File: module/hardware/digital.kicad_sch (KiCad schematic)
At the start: 36 parts, among them J10 Conn_01x03, J11 Conn_01x03, J12 Conn_01x03, J5 Conn_01x03_Male, J6 Conn_01x03_Male, J7 Conn_01x03, J8 Conn_01x03, J9 Conn_01x05_Male, SW2 SW_Push, U8 W25Q128JVS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

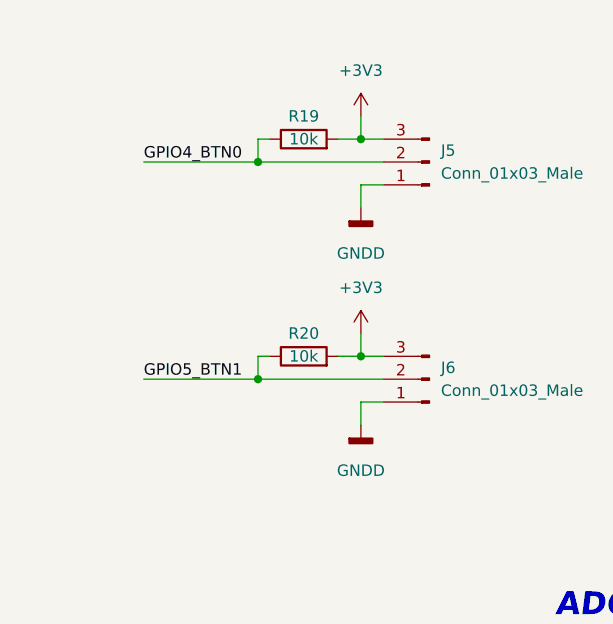
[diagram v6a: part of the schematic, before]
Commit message: Add pull down button resistor option
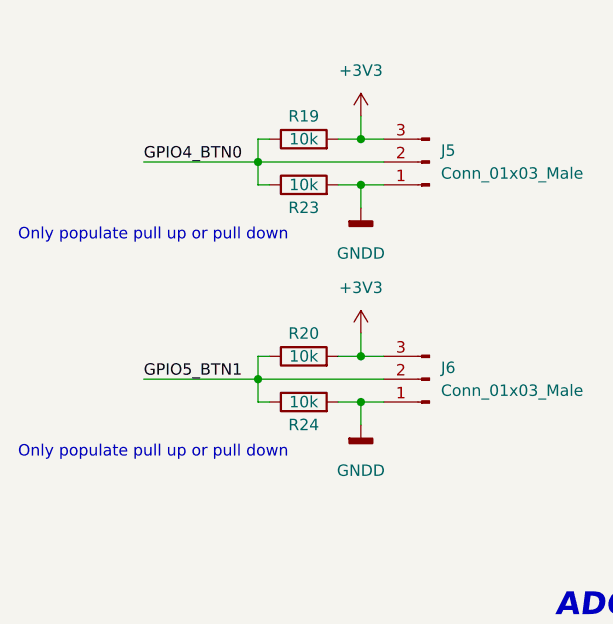
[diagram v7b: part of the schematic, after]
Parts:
- added R23, R24: 10k, Resistor_SMD:R_0603_1608Metric_Pad0.98x0.95mm_HandSolder, symbol Device:R
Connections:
- net GNDD: now also R23.2, R24.2
- net GPIO4_BTN0: now also R23.1
- net GPIO5_BTN1: now also R24.1
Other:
- note added: "Only populate pull up or pull down"
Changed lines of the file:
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@@
   (junction (at 307.34 54.61) (diameter 0) (color 0 0 0 0)
   )
+  (junction (at 69.85 64.77) (diameter 0) (color 0 0 0 0)
+  )
   (junction (at 270.51 40.64) (diameter 0) (color 0 0 0 0)
   )
@@
   )
   (junction (at 78.74 130.81) (diameter 0) (color 0 0 0 0)
+  )
+  (junction (at 69.85 88.9) (diameter 0) (color 0 0 0 0)
   )
   (junction (at 90.17 144.78) (diameter 0) (color 0 0 0 0)
@@
     (stroke (width 0) (type default) (color 0 0 0 0))
   )
+  (wire (pts (xy 58.42 64.77) (xy 59.69 64.77))
+    (stroke (width 0) (type default) (color 0 0 0 0))
+  )
   (wire (pts (xy 114.3 128.27) (xy 127 128.27))
     (stroke (width 0) (type default) (color 0 0 0 0))
@@
     (stroke (width 0) (type default) (color 0 0 0 0))
   )
+  (wire (pts (xy 67.31 88.9) (xy 69.85 88.9))
+    (stroke (width 0) (type default) (color 0 0 0 0))
+  )
   (wire (pts (xy 242.57 52.07) (xy 242.57 55.88))
     (stroke (width 0) (type default) (color 0 0 0 0))
@@
     (stroke (width 0) (type default) (color 0 0 0 0))
   )
+  (wire (pts (xy 58.42 88.9) (xy 59.69 88.9))
+    (stroke (width 0) (type default) (color 0 0 0 0))
+  )
   (wire (pts (xy 242.57 95.25) (xy 233.68 95.25))
     (stroke (width 0) (type default) (color 0 0 0 0))
@@
     (stroke (width 0) (type default) (color 0 0 0 0))
   )
+  (wire (pts (xy 58.42 62.23) (xy 58.42 64.77))
+    (stroke (width 0) (type default) (color 0 0 0 0))
+  )
   (wire (pts (xy 237.49 123.19) (xy 242.57 123.19))
     (stroke (width 0) (type default) (color 0 0 0 0))
@@
     (stroke (width 0) (type default) (color 0 0 0 0))
   )
+  (wire (pts (xy 67.31 64.77) (xy 69.85 64.77))
+    (stroke (width 0) (type default) (color 0 0 0 0))
+  )
   (wire (pts (xy 293.37 85.09) (xy 313.69 85.09))
     (stroke (width 0) (type default) (color 0 0 0 0))
@@
     (stroke (width 0) (type default) (color 0 0 0 0))
   )
+  (wire (pts (xy 58.42 86.36) (xy 58.42 88.9))
+    (stroke (width 0) (type default) (color 0 0 0 0))
+  )
   (wire (pts (xy 275.59 40.64) (xy 278.13 40.64))
     (stroke (width 0) (type default) (color 0 0 0 0))
@@
   (wire (pts (xy 144.78 120.65) (xy 144.78 123.19))
     (stroke (width 0) (type default) (color 0 0 0 0))
+  )
+  (text "Only populate pull up or pull down\n" (at 31.75 71.12 0)
+    (effects (font (size 1.27 1.27)) (justify left bottom))
   )
   (text "Optional fit.\nPlace near ADC headers" (at 71.12 128.27 0)
@@
   )
   (text "Keep routing short" (at 133.35 227.33 0)
+    (effects (font (size 1.27 1.27)) (justify left bottom))
+  )
+  (text "Only populate pull up or pull down\n" (at 31.75 95.25 0)
     (effects (font (size 1.27 1.27)) (justify left bottom))
   )
@@
     (pin "2")
     (pin "3")
+  )
+  (symbol (lib_id "Device:R") (at 63.5 64.77 90) (unit 1)
+    (in_bom yes) (on_board yes)
+    (property "Reference" "R23" (id 0) (at 63.5 67.31 90))
+    (property "Value" "10k" (id 1) (at 63.5 64.77 90))
+    (property "Footprint" "Resistor_SMD:R_0603_1608Metric_Pad0.98x0.95mm_HandSolder" (id 2) (at 63.5 66.548 90)
+      (effects (font (size 1.27 1.27)) hide)
+    )
+    (property "Datasheet" "~" (id 3) (at 63.5 64.77 0)
+      (effects (font (size 1.27 1.27)) hide)
+    )
+    (pin "1")
+    (pin "2")
   )
   (symbol (lib_id "power:+3V3") (at 144.78 120.65 0) (unit 1)
@@
       (effects (font (size 1.27 1.27)) hide)
     )
+    (pin "1")
+    (pin "2")
+  )
+  (symbol (lib_id "Device:R") (at 63.5 88.9 90) (unit 1)
+    (in_bom yes) (on_board yes)
+    (property "Reference" "R24" (id 0) (at 63.5 91.44 90))
+    (property "Value" "10k" (id 1) (at 63.5 88.9 90))
+    (property "Footprint" "Resistor_SMD:R_0603_1608Metric_Pad0.98x0.95mm_HandSolder" (id 2) (at 63.5 90.678 90)
+      (effects (font (size 1.27 1.27)) hide)
+    )
+    (property "Datasheet" "~" (id 3) (at 63.5 88.9 0)
+      (effects (font (size 1.27 1.27)) hide)
+    )

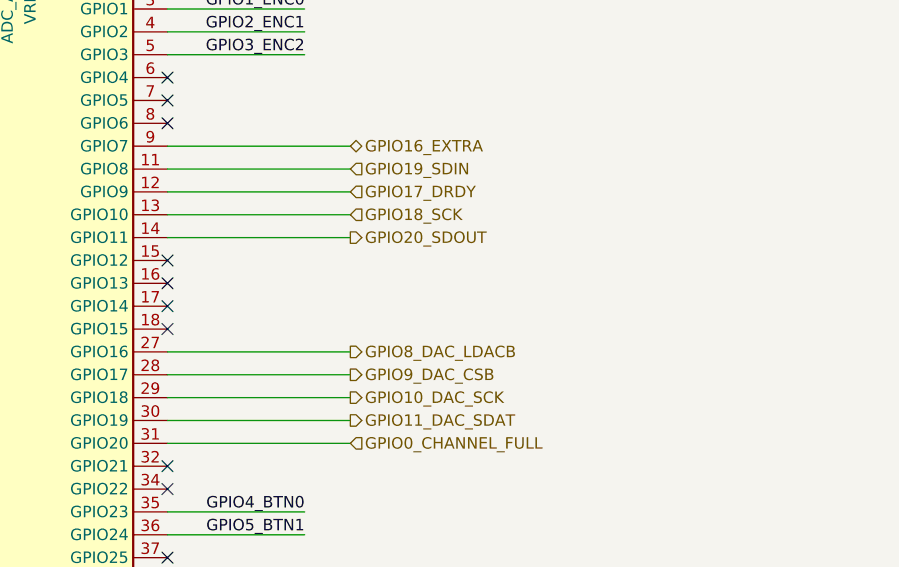
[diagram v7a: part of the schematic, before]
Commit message: Add test points; update silkscreen
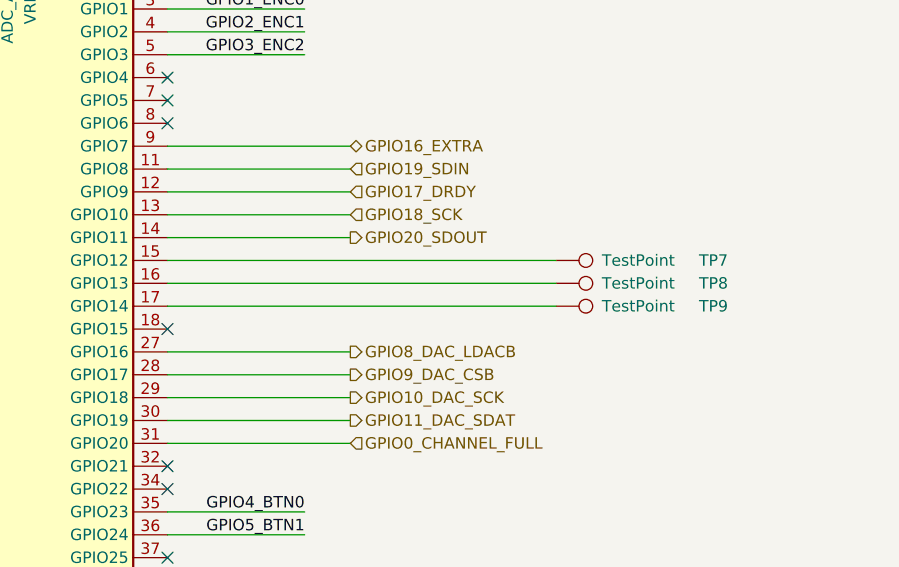
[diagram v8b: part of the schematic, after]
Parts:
- added TP7, TP8, TP9: TestPoint, TestPoint:TestPoint_Pad_D1.5mm, symbol Connector:TestPoint
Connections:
- net at U9.15 (GPIO12): now also TP7.1
- net at U9.16 (GPIO13): now also TP8.1
- net at U9.17 (GPIO14): now also TP9.1
- no-connect marks 11 -> 8
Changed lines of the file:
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@@
   (no_connect (at 293.37 120.65))
   (no_connect (at 293.37 123.19))
-  (no_connect (at 293.37 100.33))
-  (no_connect (at 293.37 97.79))
-  (no_connect (at 293.37 102.87))
   (no_connect (at 293.37 82.55))
   (wire (pts (xy 330.2 40.64) (xy 330.2 44.45))
@@
     (stroke (width 0) (type default) (color 0 0 0 0))
   )
+  (wire (pts (xy 293.37 97.79) (xy 336.55 97.79))
+    (stroke (width 0) (type default) (color 0 0 0 0))
+  )
   (wire (pts (xy 341.63 52.07) (xy 341.63 54.61))
     (stroke (width 0) (type default) (color 0 0 0 0))
@@
     (stroke (width 0) (type default) (color 0 0 0 0))
   )
+  (wire (pts (xy 293.37 100.33) (xy 336.55 100.33))
+    (stroke (width 0) (type default) (color 0 0 0 0))
+  )
   (wire (pts (xy 233.68 74.93) (xy 242.57 74.93))
     (stroke (width 0) (type default) (color 0 0 0 0))
@@
   )
   (wire (pts (xy 275.59 40.64) (xy 278.13 40.64))
+    (stroke (width 0) (type default) (color 0 0 0 0))
+  )
+  (wire (pts (xy 293.37 102.87) (xy 336.55 102.87))
     (stroke (width 0) (type default) (color 0 0 0 0))
   )
@@
     (pin "1")
   )
+  (symbol (lib_id "Connector:TestPoint") (at 336.55 97.79 270) (unit 1)
+    (in_bom yes) (on_board yes)
+    (property "Reference" "TP7" (id 0) (at 352.425 97.79 90)
+      (effects (font (size 1.27 1.27)) (justify left))
+    )
+    (property "Value" "TestPoint" (id 1) (at 341.63 97.79 90)
+      (effects (font (size 1.27 1.27)) (justify left))
+    )
+    (property "Footprint" "TestPoint:TestPoint_Pad_D1.5mm" (id 2) (at 336.55 102.87 0)
+      (effects (font (size 1.27 1.27)) hide)
+    )
+    (property "Datasheet" "~" (id 3) (at 336.55 102.87 0)
+      (effects (font (size 1.27 1.27)) hide)
+    )
+    (pin "1")
+  )
   (symbol (lib_id "Device:R") (at 233.68 123.19 90) (unit 1)
     (in_bom yes) (on_board yes) (fields_autoplaced)
@@
     )
     (property "Datasheet" "" (id 3) (at 284.48 55.88 0)
+      (effects (font (size 1.27 1.27)) hide)
+    )
+    (pin "1")
+  )
+  (symbol (lib_id "Connector:TestPoint") (at 336.55 100.33 270) (unit 1)
+    (in_bom yes) (on_board yes)
+    (property "Reference" "TP8" (id 0) (at 352.425 100.33 90)
+      (effects (font (size 1.27 1.27)) (justify left))
+    )
+    (property "Value" "TestPoint" (id 1) (at 341.63 100.33 90)
+      (effects (font (size 1.27 1.27)) (justify left))
+    )
+    (property "Footprint" "TestPoint:TestPoint_Pad_D1.5mm" (id 2) (at 336.55 105.41 0)
+      (effects (font (size 1.27 1.27)) hide)
+    )
+    (property "Datasheet" "~" (id 3) (at 336.55 105.41 0)
       (effects (font (size 1.27 1.27)) hide)
     )
@@
     (pin "2")
   )
+  (symbol (lib_id "Connector:TestPoint") (at 336.55 102.87 270) (unit 1)
+    (in_bom yes) (on_board yes)
+    (property "Reference" "TP9" (id 0) (at 352.425 102.87 90)
+      (effects (font (size 1.27 1.27)) (justify left))
+    )
+    (property "Value" "TestPoint" (id 1) (at 341.63 102.87 90)
+      (effects (font (size 1.27 1.27)) (justify left))
+    )
+    (property "Footprint" "TestPoint:TestPoint_Pad_D1.5mm" (id 2) (at 336.55 107.95 0)
+      (effects (font (size 1.27 1.27)) hide)
+    )
+    (property "Datasheet" "~" (id 3) (at 336.55 107.95 0)
+      (effects (font (size 1.27 1.27)) hide)
+    )
+    (pin "1")
+  )
   (symbol (lib_id "Device:C") (at 119.38 193.04 0) (unit 1)
